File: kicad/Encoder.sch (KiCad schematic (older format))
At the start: 4 parts, among them J10 ENC_Slave, J9 ENC_Host, U4 AS5048A

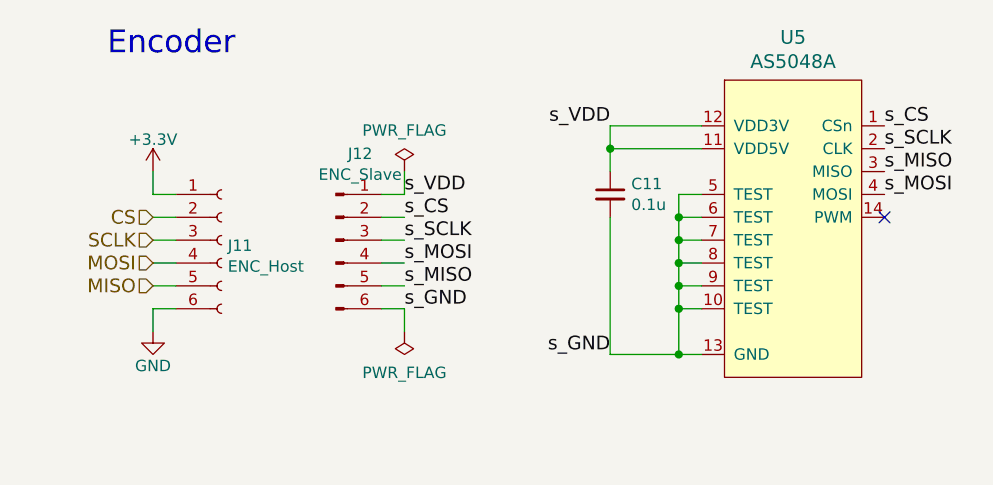
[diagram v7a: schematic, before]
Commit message: フットプリントを割り当て
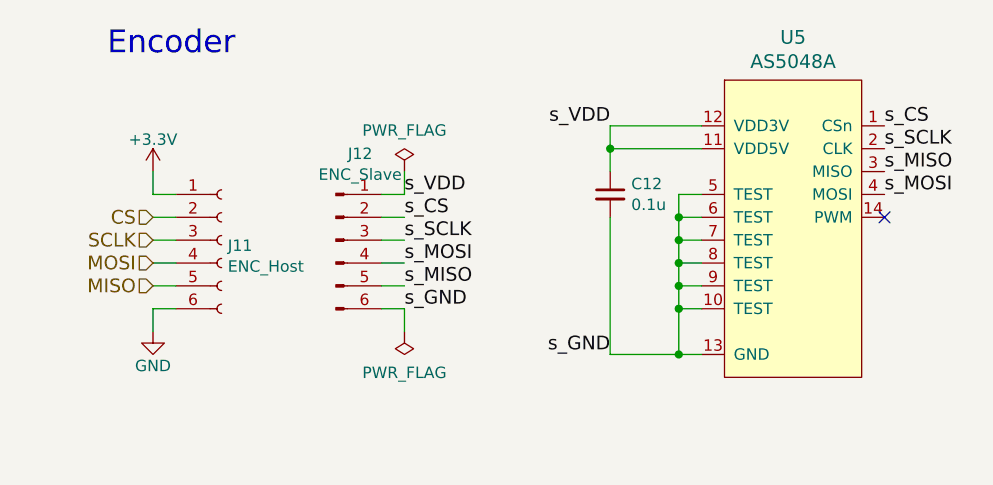
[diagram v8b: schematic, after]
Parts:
- C11: renamed from C10; footprint (none) -> Capacitor_SMD:C_0201_0603Metric
- U4: footprint (none) -> mouse:TSSOP-14_4.4x5mm_Pitch0.65mm
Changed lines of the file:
@@
 $EndDescr
 $Comp
-L power:GND #PWR048
+L power:GND #PWR050
 U 1 1 589E94E9
 P 4100 3600
-AR Path="/592ADBF2/589E94E9" Ref="#PWR048"  Part="1"
-AR Path="/59347BCD/589E94E9" Ref="#PWR050"  Part="1"
-F 0 "#PWR050" H 4100 3350 50  0001 C CNN
+AR Path="/592ADBF2/589E94E9" Ref="#PWR050"  Part="1"
+AR Path="/59347BCD/589E94E9" Ref="#PWR052"  Part="1"
+F 0 "#PWR052" H 4100 3350 50  0001 C CNN
 F 1 "GND" H 4100 3450 50  0000 C CNN
 F 2 "" H 4100 3600 50  0000 C CNN
@@
 $EndComp
 $Comp
-L power:+3.3V #PWR047
+L power:+3.3V #PWR049
 U 1 1 589CCACF
 P 4100 2900
-AR Path="/592ADBF2/589CCACF" Ref="#PWR047"  Part="1"
-AR Path="/59347BCD/589CCACF" Ref="#PWR049"  Part="1"
-F 0 "#PWR049" H 4100 2750 50  0001 C CNN
+AR Path="/592ADBF2/589CCACF" Ref="#PWR049"  Part="1"
+AR Path="/59347BCD/589CCACF" Ref="#PWR051"  Part="1"
+F 0 "#PWR051" H 4100 2750 50  0001 C CNN
 F 1 "+3.3V" H 4100 3040 50  0000 C CNN
 F 2 "" H 4100 2900 50  0000 C CNN
@@
 F 0 "U5" H 6900 3687 60  0000 C CNN
 F 1 "AS5048A" H 6900 3581 60  0000 C CNN
-F 2 "" H 6900 3400 60  0000 C CNN
+F 2 "mouse:TSSOP-14_4.4x5mm_Pitch0.65mm" H 6900 3400 60  0001 C CNN
 F 3 "" H 6900 3400 60  0000 C CNN
 	1    6900 3000
@@
 s_VDD
 $Comp
-L Device:C_Small C10
+L Device:C_Small C11
 U 1 1 5C2A3C19
 P 6100 3000
-AR Path="/592ADBF2/5C2A3C19" Ref="C10"  Part="1"
-AR Path="/59347BCD/5C2A3C19" Ref="C11"  Part="1"
-F 0 "C11" H 6192 3046 50  0000 L CNN
+AR Path="/592ADBF2/5C2A3C19" Ref="C11"  Part="1"
+AR Path="/59347BCD/5C2A3C19" Ref="C12"  Part="1"
+F 0 "C12" H 6192 3046 50  0000 L CNN
 F 1 "0.1u" H 6192 2955 50  0000 L CNN
-F 2 "" H 6100 3000 50  0001 C CNN
+F 2 "Capacitor_SMD:C_0201_0603Metric" H 6100 3000 50  0001 C CNN
 F 3 "~" H 6100 3000 50  0001 C CNN
 	1    6100 3000
